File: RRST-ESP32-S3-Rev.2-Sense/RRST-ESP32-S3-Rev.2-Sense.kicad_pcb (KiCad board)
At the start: 4 copper layers, 40.7 x 56.9 mm, 77 parts, among them J1 Conn_01x22_Pin, J10 Conn_01x02_Socket, J11 Conn_01x02_Socket, J12 Conn_01x02_Socket, J2 USB_C_Receptacle_USB2.0_16P, J3 Conn_01x22_Pin, J4 Conn_01x04_Socket, J5 Conn_01x04_Socket, J6 Conn_01x04_Socket, J7 Conn_01x04_Socket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

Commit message: 仮配置
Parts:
- removed D10, D11, D12, D13, D14, D15, D16, D17, D18, D19, D20, D21, D7, D9: LED, LED_SMD:LED_0603_1608Metric
- removed R10, R11, R12, R13, R14, R15, R16, R17, R18, R19, R20, R21, R22, R9: 330, Resistor_SMD:R_0603_1608Metric
- removed REF**104: MountingHole_3.2mm_M3, MountingHole:MountingHole_3.2mm_M3
- J10, J11, J12, J9: footprint Connector_JST:JST_XH_S2B-XH-A-1_1x02_P2.50mm_Horizontal -> Connector_JST:JST_XH_B2B-XH-A_1x02_P2.50mm_Vertical
- J4, J8: footprint Connector_JST:JST_XH_S4B-XH-A-1_1x04_P2.50mm_Horizontal -> Connector_JST:JST_XH_B4B-XH-A_1x04_P2.50mm_Vertical
- moved J12 27.9 mm to (102.1, 87.1), turned to -90 degrees
- moved J5 24.5 mm to (67.6, 123.9)
- moved J9 23.5 mm to (102.1, 113.0), turned to -90 degrees
- moved J4 21.1 mm to (67.6, 108.1), turned to 90 degrees
- moved J6 14.6 mm to (102.4, 121.4), turned to -90 degrees
- moved J11 10.8 mm to (102.1, 95.8), turned to -90 degrees
- moved J7 7.94 mm to (86.4, 123.4), turned to 180 degrees
- moved J10 6.42 mm to (102.1, 104.4), turned to -90 degrees
- moved J8 6.20 mm to (67.6, 94.5), turned to 90 degrees
- renumbered ↓TERM to R8
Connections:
- J5 pad 3: CAN_TX -> CANH
- J5 pad 4: CAN_RX -> CANL
- J6 pad 3: CAN_TX -> CANH
- J6 pad 4: CAN_RX -> CANL
- J7 pad 3: CAN_TX -> CANH
- J7 pad 4: CAN_RX -> CANL
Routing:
- net (no net): track 0.00 -> 11.7 mm
- net CANL: track 12.4 -> 17.5 mm
- net CAN_RX: track 66.0 -> 61.1 mm
- net 5V0: track 124.6 -> 128.6 mm
- net GND: track 81.2 -> 84.0 mm
- net Net-(D15-K): track 1.49 -> 0.00 mm
- net Net-(D14-K): track 1.49 -> 0.00 mm
- net Net-(D12-K): track 1.49 -> 0.00 mm
- net Net-(D13-K): track 1.49 -> 0.00 mm
- net Net-(D9-K): track 1.44 -> 0.00 mm
- net Net-(D7-K): track 1.44 -> 0.00 mm
- net Net-(D11-K): track 1.44 -> 0.00 mm
- net Net-(D10-K): track 1.44 -> 0.00 mm
- net Net-(D20-K): track 1.41 -> 0.00 mm
- net Net-(D19-K): track 1.41 -> 0.00 mm
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
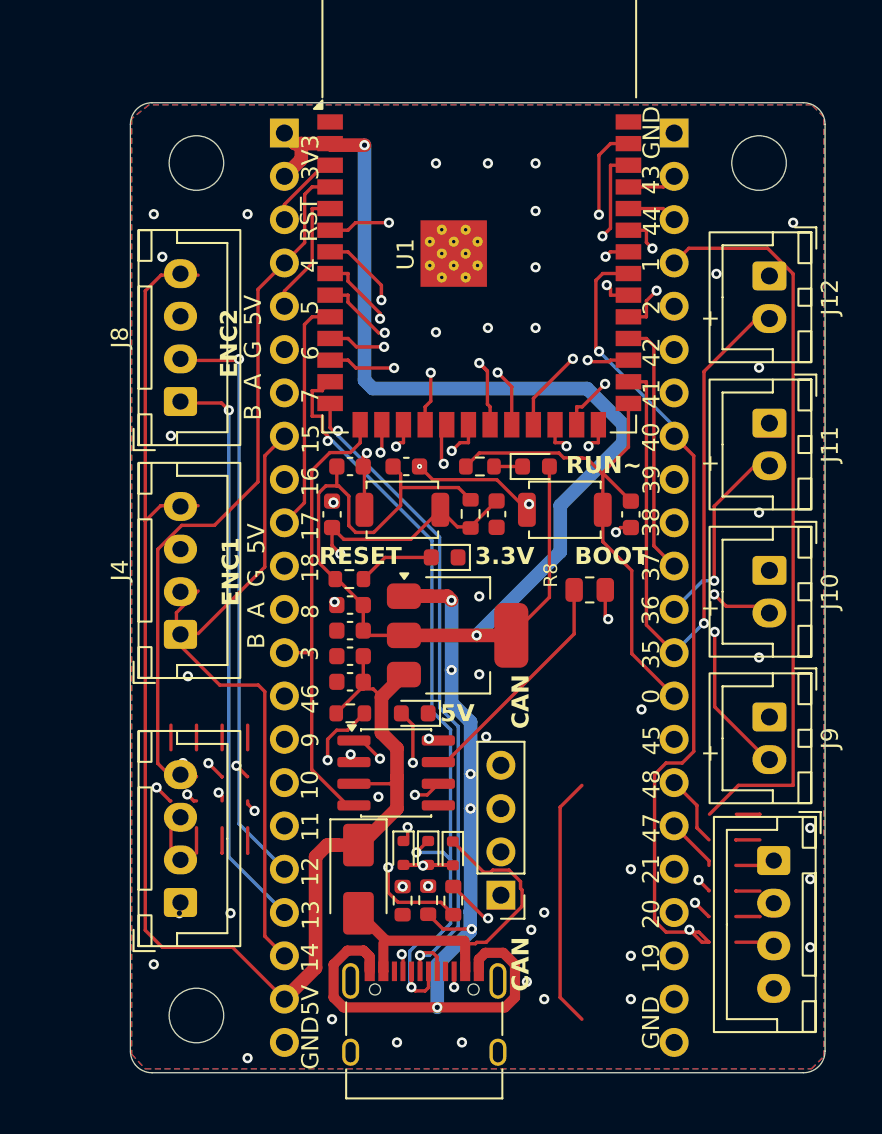
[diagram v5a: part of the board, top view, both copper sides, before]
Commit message: 仮配置完了、拡張基板設計開始
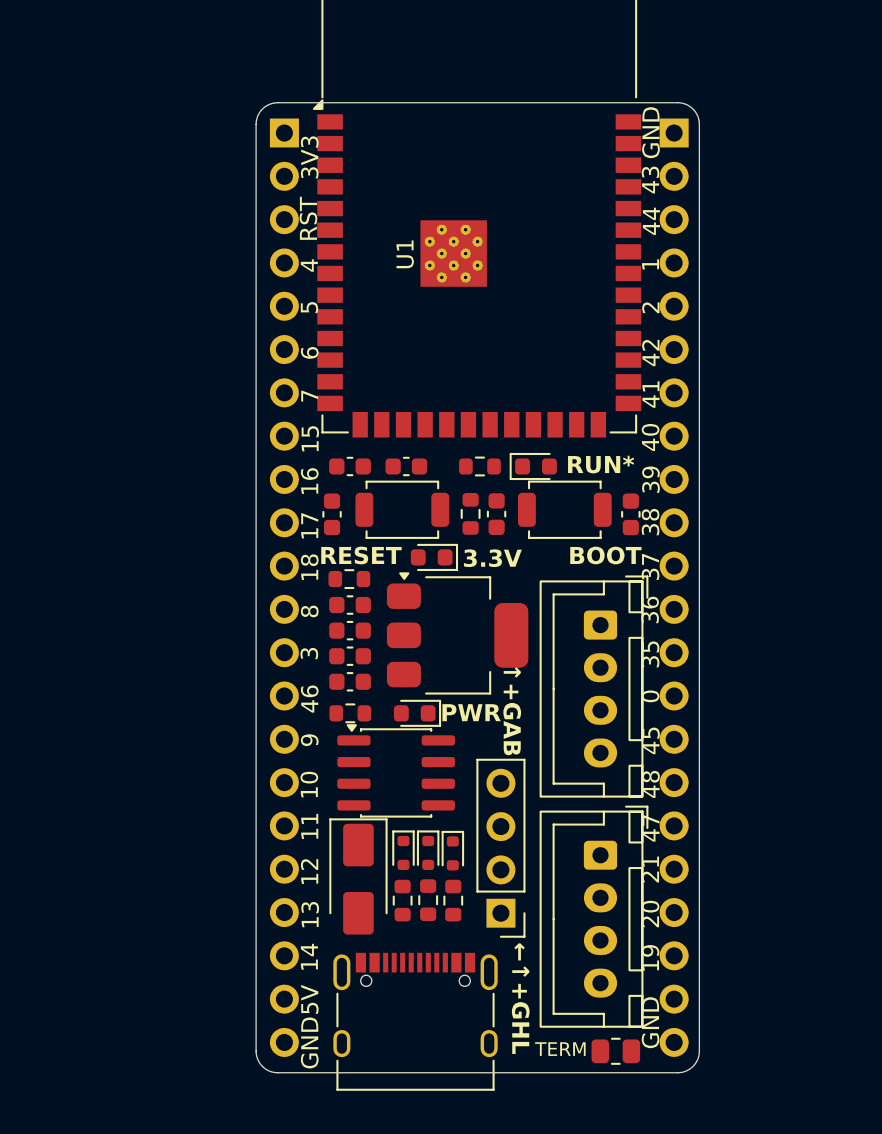
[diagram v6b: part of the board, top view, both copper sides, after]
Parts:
- removed J10, J11, J12, J9: Conn_01x02_Socket, Connector_JST:JST_XH_B2B-XH-A_1x02_P2.50mm_Vertical
- removed J5, J8: Conn_01x04_Socket, Connector_JST:JST_XH_B4B-XH-A_1x04_P2.50mm_Vertical
- removed REF**, REF**102, REF**103: MountingHole_3.2mm_M3, MountingHole:MountingHole_3.2mm_M3
- moved TERM 27.1 mm to (93.1, 132.6), turned to 180 degrees
- moved J4 24.6 mm to (92.2, 107.6), turned to -90 degrees
- moved J6 10.2 mm to (92.2, 121.1)
- moved J7 1.06 mm to (86.4, 124.5)
- moved D4 0.76 mm to (82.3, 103.6)
- moved J2 0.72 mm to (81.3, 131.1)
- renumbered R8 to TERM
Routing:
- net 5V0: track 128.6 -> 0.00 mm, vias 1 -> 0
- net 3V3: track 97.9 -> 0.00 mm, vias 2 -> 0
- net GND: track 84.0 -> 0.00 mm, vias 51 -> 0
- net CAN_TX: track 76.0 -> 0.00 mm, vias 2 -> 0
- net ENC1_B: track 75.0 -> 0.00 mm, vias 2 -> 0
- net ENC2_A: track 69.1 -> 0.00 mm, vias 2 -> 0
- net DP: track 68.5 -> 0.00 mm, vias 3 -> 0
- net DN: track 66.8 -> 0.00 mm, vias 3 -> 0
- net ENC1_A: track 64.6 -> 0.00 mm, vias 2 -> 0
- net CAN_RX: track 61.1 -> 0.00 mm
- net IO1: track 54.9 -> 0.00 mm, vias 1 -> 0
- net IO41: track 48.9 -> 0.00 mm, vias 2 -> 0
- net IO40: track 48.7 -> 0.00 mm, vias 2 -> 0
- net IO42: track 45.1 -> 0.00 mm, vias 2 -> 0
- net IO6: track 43.0 -> 0.00 mm, vias 2 -> 0
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- removed copper zone on B.Cu, net GND
- removed copper zone on F.Cu, net GND
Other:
- board size 40.7 x 56.9 mm -> 26 x 56.9 mm
- board text added: "PWR"
- board text added: "RUN*"
- board text added: "←↑+GHL"
- board text added: "↑+GAB"
- board text removed: "+"
- board text removed: "B A G 5V"
- board text removed: "CAN"
- board text removed: "ENC1"
- board text removed: "ENC2"
- board text removed: "RUN~"

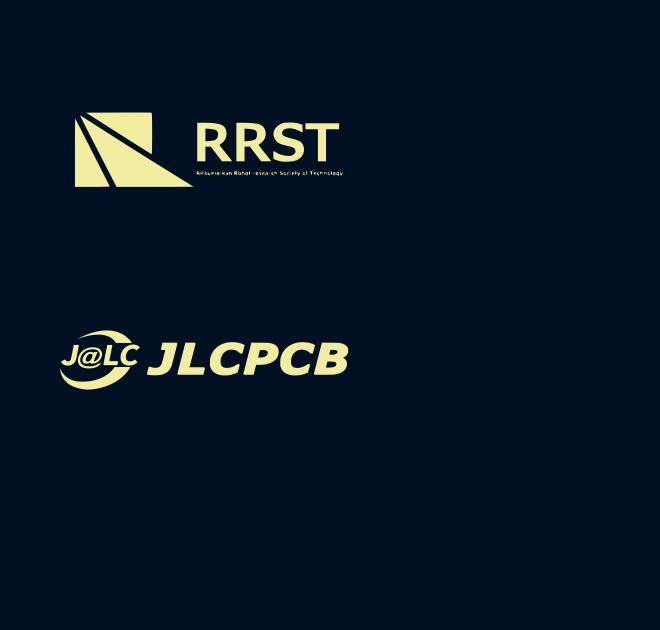
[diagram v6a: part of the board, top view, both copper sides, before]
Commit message: 拡張基板、外形線
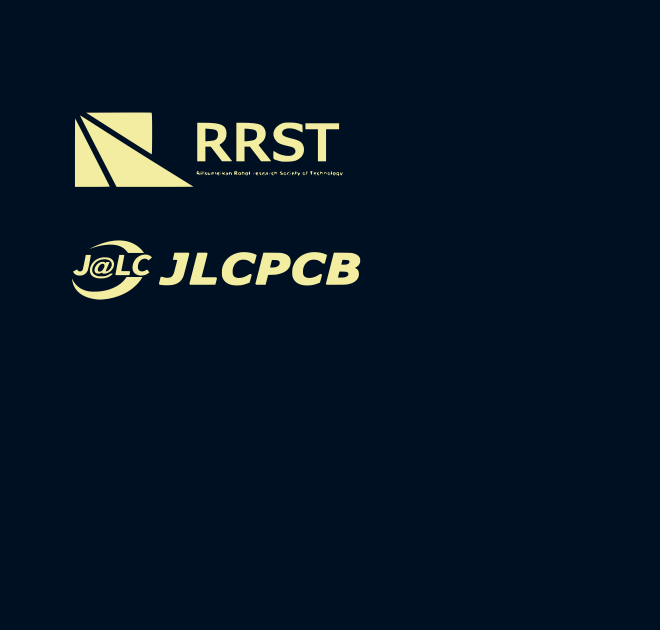
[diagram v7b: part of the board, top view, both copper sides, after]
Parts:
- moved G***_3 3.03 mm to (44.5, 113.2)
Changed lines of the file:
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@@
 	(footprint "LOGO"
 		(layer "F.Cu")
-		(at 44.1 116.2)
+		(at 44.5 113.2)
 		(property "Reference" "G***_3"
 			(at 0 0 0)
